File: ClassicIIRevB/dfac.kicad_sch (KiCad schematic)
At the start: 34 parts, among them U4 DFAC_343S1033

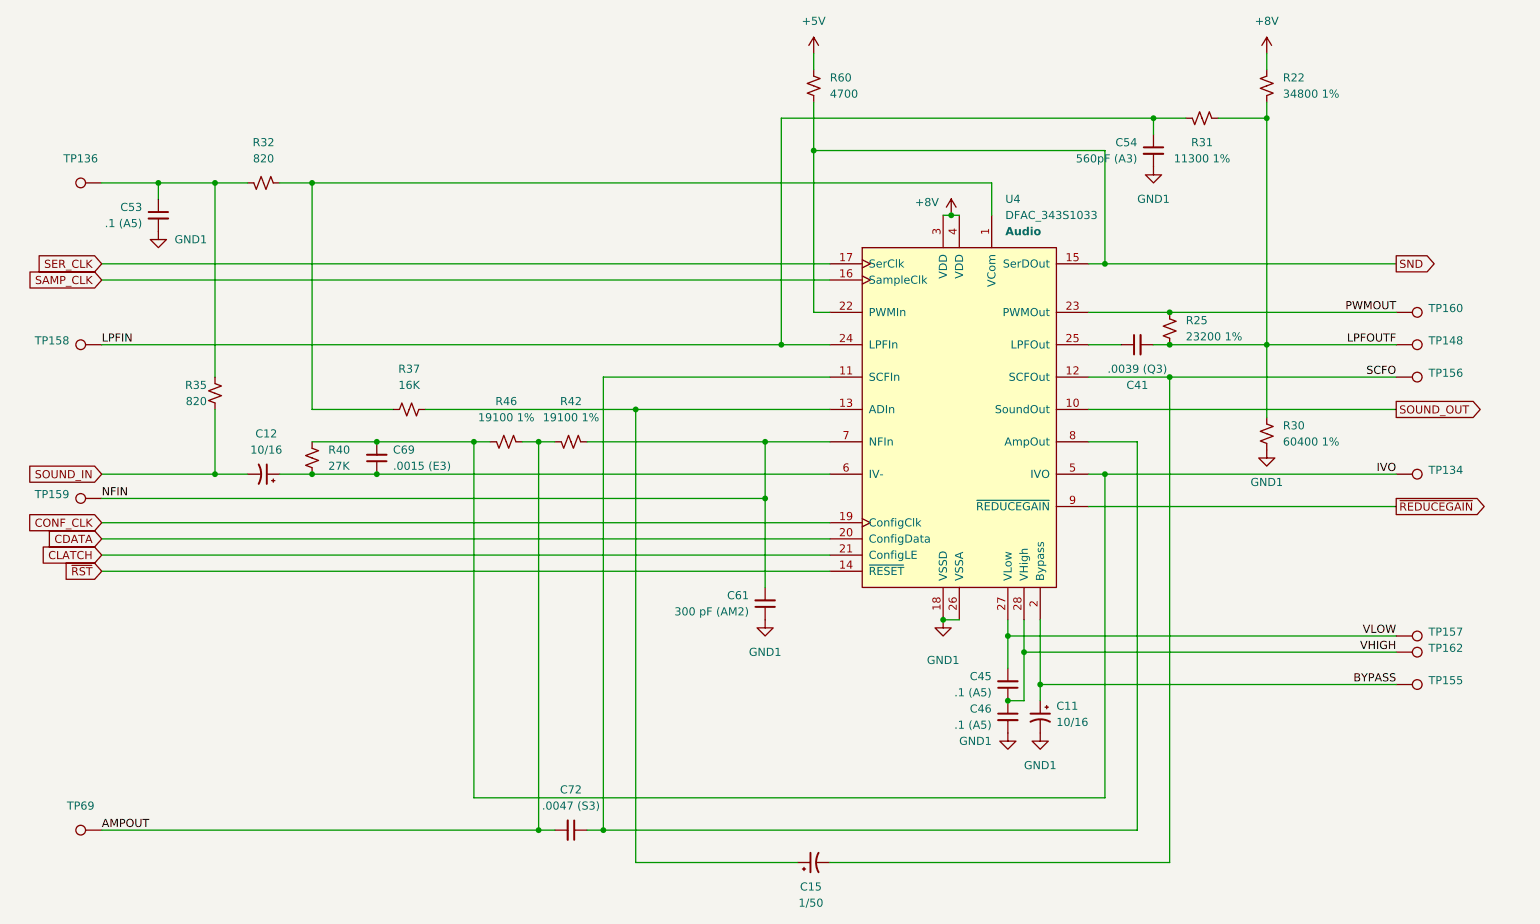
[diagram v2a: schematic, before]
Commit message: Switch to some "official" net names
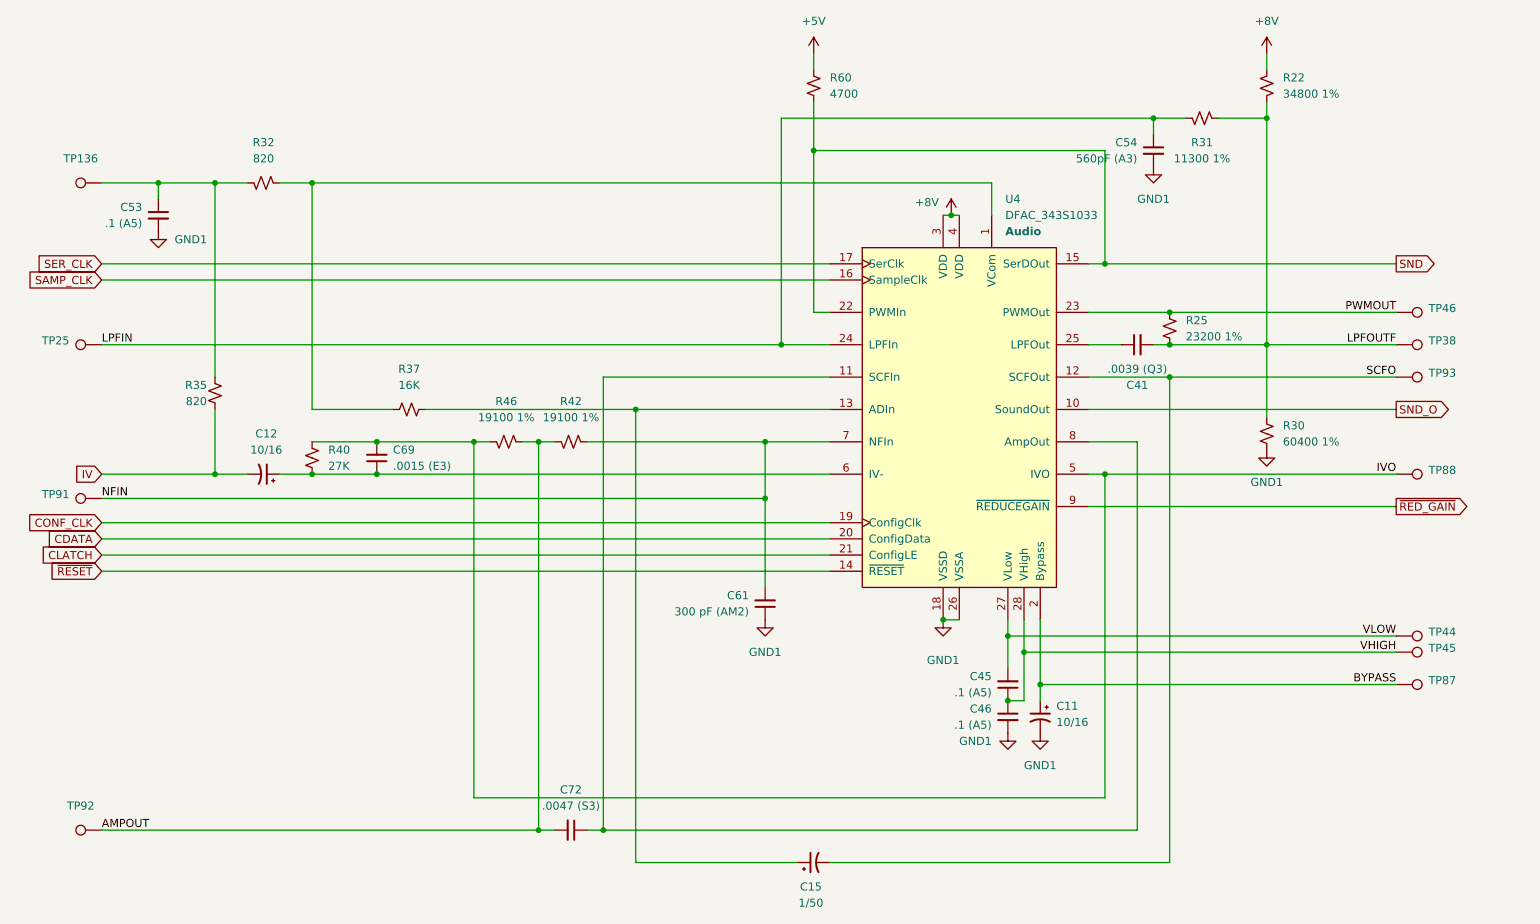
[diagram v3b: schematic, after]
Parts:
- renumbered TP158 to TP25, TP148 to TP38, TP157 to TP44, TP162 to TP45, TP160 to TP46, TP155 to TP87, TP134 to TP88, TP159 to TP91, TP69 to TP92, TP156 to TP93
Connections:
- net SOUND_IN renamed IV
- net SOUND_OUT renamed SND_O
- net ~{REDUCEGAIN} renamed ~{RED_GAIN}
- net ~{RST} renamed ~{RESET}
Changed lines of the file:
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@@
 		)
 	)
-	(global_label "SOUND_IN"
+	(global_label "IV"
 		(shape input)
 		(at 38.1 104.14 180)
@@
 		)
 		(property "Intersheetrefs" "${INTERSHEET_REFS}"
-			(at 25.7409 104.14 0)
+			(at 33.4214 104.14 0)
 			(effects
 				(font
@@
 		)
 	)
-	(global_label "~{REDUCEGAIN}"
+	(global_label "~{RED_GAIN}"
 		(shape output)
 		(at 241.3 109.22 0)
@@
 		)
 		(property "Intersheetrefs" "${INTERSHEET_REFS}"
-			(at 256.0176 109.22 0)
-			(effects
-				(font
-					(size 1.27 1.27)
-				)
-				(justify left)
-			)
-		)
-	)
-	(global_label "SOUND_OUT"
+			(at 253.2357 109.22 0)
+			(effects
+				(font
+					(size 1.27 1.27)
+				)
+				(justify left)
+			)
+		)
+	)
+	(global_label "SND_O"
 		(shape output)
 		(at 241.3 93.98 0)
@@
 		)
 		(property "Intersheetrefs" "${INTERSHEET_REFS}"
-			(at 255.3524 93.98 0)
-			(effects
-				(font
-					(size 1.27 1.27)
-				)
-				(justify left)
-			)
-		)
-	)
-	(global_label "~{RST}"
+			(at 250.3933 93.98 0)
+			(effects
+				(font
+					(size 1.27 1.27)
+				)
+				(justify left)
+			)
+		)
+	)
+	(global_label "~{RESET}"
 		(shape input)
 		(at 38.1 119.38 180)
@@
 		)
 		(property "Intersheetrefs" "${INTERSHEET_REFS}"
-			(at 31.6677 119.38 0)
+			(at 29.3697 119.38 0)
 			(effects
 				(font
@@
 		(dnp no)
 		(fields_autoplaced yes)
-		(property "Reference" "TP155"
+		(property "Reference" "TP87"
 			(at 246.38 136.5249 90)
 			(effects
@@
 			(project "ClassicIIRevB"
 				(path "/08c23af6-72f1-4a8f-a60c-b986fe71300f/e3fee5a1-cf40-4697-883d-e8942f3ad207"
-					(reference "TP155")
+					(reference "TP87")
 					(unit 1)
 				)
@@
 		(dnp no)
 		(fields_autoplaced yes)
-		(property "Reference" "TP162"
+		(property "Reference" "TP45"
 			(at 246.38 131.4449 90)
 			(effects
@@
 			(project "ClassicIIRevB"
 				(path "/08c23af6-72f1-4a8f-a60c-b986fe71300f/e3fee5a1-cf40-4697-883d-e8942f3ad207"
-					(reference "TP162")
+					(reference "TP45")
 					(unit 1)
 				)
@@
 		(on_board yes)
 		(dnp no)
-		(property "Reference" "TP158"
+		(property "Reference" "TP25"
 			(at 33.02 83.1849 90)
 			(effects
@@
 			(project "ClassicIIRevB"
 				(path "/08c23af6-72f1-4a8f-a60c-b986fe71300f/e3fee5a1-cf40-4697-883d-e8942f3ad207"
-					(reference "TP158")
+					(reference "TP25")
 					(unit 1)
 				)
@@
 		(dnp no)
 		(fields_autoplaced yes)
-		(property "Reference" "TP148"
+		(property "Reference" "TP38"
 			(at 246.38 83.1849 90)
 			(effects
@@
 			(project "ClassicIIRevB"
 				(path "/08c23af6-72f1-4a8f-a60c-b986fe71300f/e3fee5a1-cf40-4697-883d-e8942f3ad207"
-					(reference "TP148")
+					(reference "TP38")
 					(unit 1)
 				)
@@
 		(dnp no)
 		(fields_autoplaced yes)
-		(property "Reference" "TP159"
+		(property "Reference" "TP91"
 			(at 33.02 107.3149 90)
 			(effects
@@
 			(project "ClassicIIRevB"
 				(path "/08c23af6-72f1-4a8f-a60c-b986fe71300f/e3fee5a1-cf40-4697-883d-e8942f3ad207"
-					(reference "TP159")
+					(reference "TP91")
 					(unit 1)
 				)
@@
 		(dnp no)
 		(fields_autoplaced yes)
-		(property "Reference" "TP69"
+		(property "Reference" "TP92"
 			(at 34.798 156.21 90)
 			(effects
@@
 			(project "ClassicIIRevB"
 				(path "/08c23af6-72f1-4a8f-a60c-b986fe71300f/e3fee5a1-cf40-4697-883d-e8942f3ad207"
-					(reference "TP69")
+					(reference "TP92")
 					(unit 1)
 				)
@@
 		(dnp no)
 		(fields_autoplaced yes)
-		(property "Reference" "TP156"
+		(property "Reference" "TP93"
 			(at 246.38 88.2649 90)
 			(effects
@@
 			(project "ClassicIIRevB"
 				(path "/08c23af6-72f1-4a8f-a60c-b986fe71300f/e3fee5a1-cf40-4697-883d-e8942f3ad207"
-					(reference "TP156")
+					(reference "TP93")
 					(unit 1)
 				)
@@
 		(dnp no)
 		(fields_autoplaced yes)
-		(property "Reference" "TP134"
+		(property "Reference" "TP88"
 			(at 246.38 103.5049 90)
 			(effects
@@
 			(project "ClassicIIRevB"
 				(path "/08c23af6-72f1-4a8f-a60c-b986fe71300f/e3fee5a1-cf40-4697-883d-e8942f3ad207"
-					(reference "TP134")
+					(reference "TP88")
 					(unit 1)
 				)
@@
 		(dnp no)
 		(fields_autoplaced yes)
-		(property "Reference" "TP160"
+		(property "Reference" "TP46"
 			(at 246.38 78.1049 90)
 			(effects
@@
 			(project "ClassicIIRevB"
 				(path "/08c23af6-72f1-4a8f-a60c-b986fe71300f/e3fee5a1-cf40-4697-883d-e8942f3ad207"
-					(reference "TP160")
+					(reference "TP46")
 					(unit 1)
 				)
@@
 		(dnp no)
 		(fields_autoplaced yes)
-		(property "Reference" "TP157"
+		(property "Reference" "TP44"
 			(at 246.38 128.9049 90)
 			(effects
@@
 			(project "ClassicIIRevB"
 				(path "/08c23af6-72f1-4a8f-a60c-b986fe71300f/e3fee5a1-cf40-4697-883d-e8942f3ad207"
-					(reference "TP157")
-					(unit 1)
-				)
+					(reference "TP44")
+					(unit 1)
+				)

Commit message: update exports
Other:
- title: Macintosh Classic II Revision B -> Macintosh Classic II (Later Revision)
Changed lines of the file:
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@@
 	(paper "USLetter")
 	(title_block
-		(title "Macintosh Classic II Revision B")
-		(date "2025-06-04")
+		(title "Macintosh Classic II (Later Revision)")
+		(date "2025-06-16")
 		(company "Apple Computer")
 		(comment 1 "drawn by Bradley Bell")

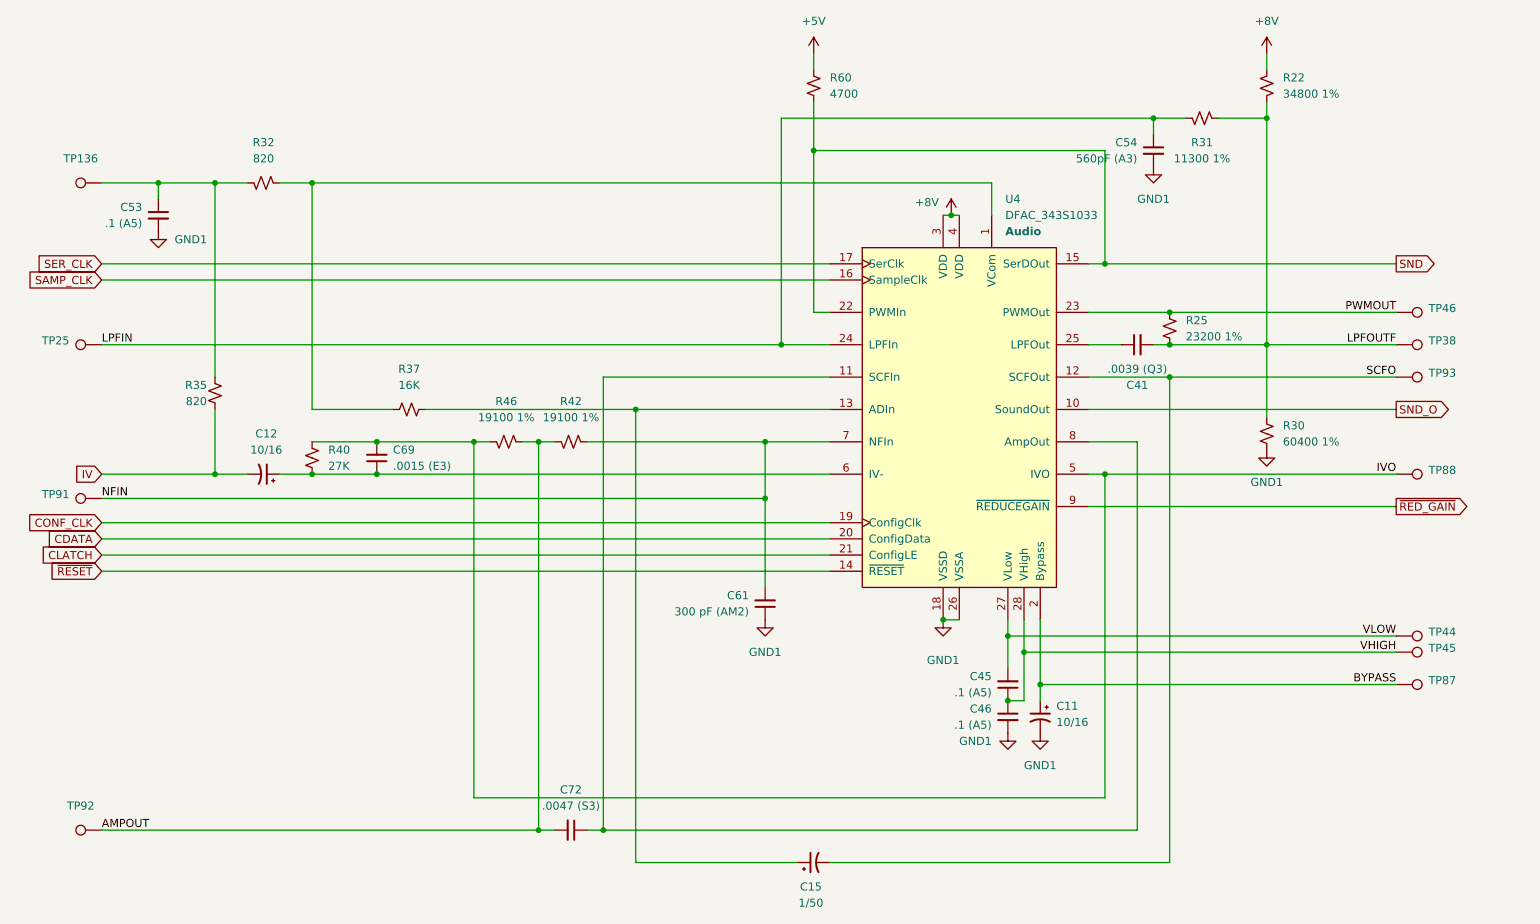
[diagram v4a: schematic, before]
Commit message: Corrections to SMDs, more improved footprints
The later revision board reproduction design is now complete.
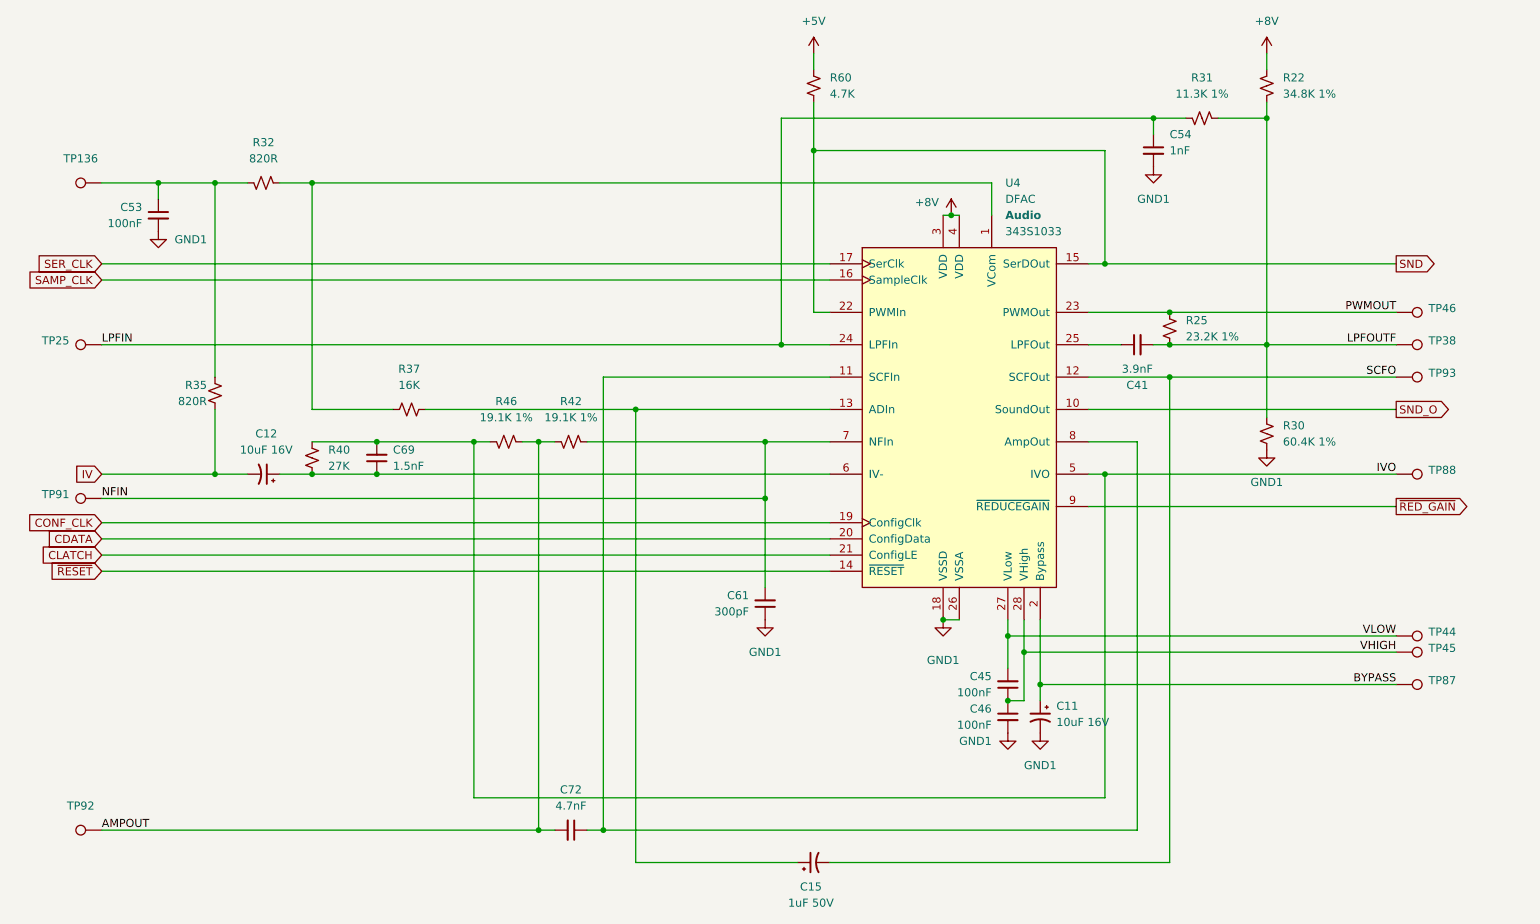
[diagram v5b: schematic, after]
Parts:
- C11, C12: value 10/16 -> 10uF 16V
- C15: value 1/50 -> 1uF 50V
- C41: value .0039 (Q3) -> 3.9nF
- C45, C46, C53: value .1 (A5) -> 100nF
- C54: value 560pF (A3) -> 1nF
- C61: value 300 pF (AM2) -> 300pF
- C69: value .0015 (E3) -> 1.5nF
- C72: value .0047 (S3) -> 4.7nF
- R22: value 34800 1% -> 34.8K 1%
- R25: value 23200 1% -> 23.2K 1%
- R30: value 60400 1% -> 60.4K 1%
- R31: value 11300 1% -> 11.3K 1%
- R32, R35: value 820 -> 820R
- R42, R46: value 19100 1% -> 19.1K 1%
- R60: value 4700 -> 4.7K
- TP136, TP25, TP38, TP44, TP45, TP46, TP87, TP88, TP91, TP92, TP93: now left out of the parts list
- U4: value DFAC_343S1033 -> DFAC; PartNum (none) -> 343S1033
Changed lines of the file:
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@@
 	(title_block
 		(title "Macintosh Classic II (Later Revision)")
-		(date "2025-06-16")
+		(date "2025-06-21")
 		(company "Apple Computer")
 		(comment 1 "drawn by Bradley Bell")
@@
 			)
 		)
-		(property "Value" "19100 1%"
+		(property "Value" "19.1K 1%"
 			(at 111.76 95.25 90)
 			(effects
@@
 		(unit 1)
 		(exclude_from_sim no)
-		(in_bom yes)
+		(in_bom no)
 		(on_board yes)
 		(dnp no)
@@
 			)
 		)
-		(property "Value" "23200 1%"
+		(property "Value" "23.2K 1%"
 			(at 208.28 82.5499 0)
 			(effects
@@
 		(fields_autoplaced yes)
 		(property "Reference" "C54"
-			(at 200.66 52.0762 0)
+			(at 205.74 50.8062 0)
 			(effects
 				(font
 					(size 1.27 1.27)
 				)
-				(justify right)
+				(justify left)
 			)
 		)
-		(property "Value" "560pF (A3)"
-			(at 200.66 54.6162 0)
+		(property "Value" "1nF"
+			(at 205.74 53.3462 0)
 			(effects
 				(font
 					(size 1.27 1.27)
 				)
-				(justify right)
+				(justify left)
 			)
 		)
@@
 			)
 		)
-		(property "Value" ".1 (A5)"
+		(property "Value" "100nF"
 			(at 177.8 138.4235 0)
 			(effects
@@
 		(unit 1)
 		(exclude_from_sim no)
-		(in_bom yes)
+		(in_bom no)
 		(on_board yes)
 		(dnp no)
@@
 		(unit 1)
 		(exclude_from_sim no)
-		(in_bom yes)
+		(in_bom no)
 		(on_board yes)
 		(dnp no)
@@
 			)
 		)
-		(property "Value" ".0039 (Q3)"
+		(property "Value" "3.9nF"
 			(at 200.6663 87.63 90)
 			(effects
@@
 		(unit 1)
 		(exclude_from_sim no)
-		(in_bom yes)
+		(in_bom no)
 		(on_board yes)
 		(dnp no)
@@
 		(unit 1)
 		(exclude_from_sim no)
-		(in_bom yes)
+		(in_bom no)
 		(on_board yes)
 		(dnp no)
@@
 			)
 		)
-		(property "Value" ".0047 (S3)"
+		(property "Value" "4.7nF"
 			(at 111.7536 156.21 90)
 			(effects
@@
 		(unit 1)
 		(exclude_from_sim no)
-		(in_bom yes)
+		(in_bom no)
 		(on_board yes)
 		(dnp no)
@@
 			)
 		)
-		(property "Value" ".1 (A5)"
+		(property "Value" "100nF"
 			(at 177.8 143.5162 0)
 			(effects
@@
 			)
 		)
-		(property "Value" "300 pF (AM2)"
+		(property "Value" "300pF"
 			(at 139.7 125.7235 0)
 			(effects
@@
 			)
 		)
-		(property "Value" "4700"
+		(property "Value" "4.7K"
 			(at 152.4 44.4499 0)
 			(effects
@@
 			)
 		)
-		(property "Value" ".0015 (E3)"
+		(property "Value" "1.5nF"
 			(at 83.82 102.8635 0)
 			(effects
@@
 			)
 		)
-		(property "Value" "19100 1%"
+		(property "Value" "19.1K 1%"
 			(at 101.6 95.25 90)
 			(effects
@@
 			)
 		)
-		(property "Value" "1/50"
+		(property "Value" "1uF 50V"
 			(at 149.4282 171.45 90)
 			(effects
@@
 		(unit 1)
 		(exclude_from_sim no)
-		(in_bom yes)
+		(in_bom no)
 		(on_board yes)
 		(dnp no)
@@
 			)
 		)
-		(property "Value" "60400 1%"
+		(property "Value" "60.4K 1%"
 			(at 223.52 99.0599 0)
 			(effects
@@
 		(fields_autoplaced yes)
 		(property "Reference" "U4"
-			(at 179.9433 60.96 0)
+			(at 179.9433 58.42 0)
 			(effects
 				(font
@@
 			)
 		)
-		(property "Value" "DFAC_343S1033"
-			(at 179.9433 63.5 0)
+		(property "Value" "DFAC"
+			(at 179.9433 60.96 0)
 			(effects
 				(font
@@
 		)
 		(property "Description" "Audio"
-			(at 179.9433 66.04 0)
+			(at 179.9433 63.5 0)
 			(effects
 				(font
@@
 			)
 		)
+		(property "PartNum" "343S1033"
+			(at 179.9433 66.04 0)
+			(effects
+				(font
+					(size 1.27 1.27)
+				)
+				(justify left)
+			)
+		)
 		(pin "8"
 		)
@@
 			)
 		)
-		(property "Value" "820"
+		(property "Value" "820R"
 			(at 54.61 92.7099 0)
 			(effects
@@
 			)
 		)
-		(property "Value" "820"
+		(property "Value" "820R"
 			(at 63.5 54.61 90)
 			(effects
@@
 		(unit 1)
 		(exclude_from_sim no)
-		(in_bom yes)
+		(in_bom no)
 		(on_board yes)
 		(dnp no)
@@
 		(unit 1)
 		(exclude_from_sim no)
-		(in_bom yes)
+		(in_bom no)
 		(on_board yes)
 		(dnp no)
@@
 			)
 		)
-		(property "Value" "10/16"
+		(property "Value" "10uF 16V"
 			(at 63.9318 100.33 90)
 			(effects
@@
 		(fields_autoplaced yes)
 		(property "Reference" "R31"
-			(at 210.82 52.07 90)
+			(at 210.82 41.91 90)
 			(effects
 				(font
@@
 			)
 		)
-		(property "Value" "11300 1%"
-			(at 210.82 54.61 90)
+		(property "Value" "11.3K 1%"
+			(at 210.82 44.45 90)
 			(effects
 				(font
@@
 		(unit 1)
 		(exclude_from_sim no)
-		(in_bom yes)
+		(in_bom no)
 		(on_board yes)
 		(dnp no)
@@
 			)
 		)
-		(property "Value" "34800 1%"
+		(property "Value" "34.8K 1%"
 			(at 223.52 44.4499 0)
 			(effects
@@
 			)
 		)
-		(property "Value" ".1 (A5)"
+		(property "Value" "100nF"
 			(at 44.45 64.7762 0)
 			(effects
@@
 		(unit 1)
 		(exclude_from_sim no)
-		(in_bom yes)
+		(in_bom no)
 		(on_board yes)
 		(dnp no)
@@
 			)
 		)
-		(property "Value" "10/16"
+		(property "Value" "10uF 16V"
 			(at 187.96 143.0781 0)
 			(effects
